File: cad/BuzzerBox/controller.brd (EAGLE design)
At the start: 100 x 100 mm, 132 parts, among them J2 RASPBERRYPI-40-PIN-GPIO_PTH_N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, Q1 BSS138, Q2 BSS138, Q3 BSS138, T1 BC849, T10 BC849, T2 BC849, T3 BC849, T4 BC849, T5 BC849, T6 BC849, T7 BC849, T8 BC849, T9 BC849, U1 ATMEGA328P-AU, Y1 16MHz

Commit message: Pull back internal layers around non plated drill holes
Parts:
- renumbered U$5 to U$4
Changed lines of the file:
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@@
 <element name="U$2" library="WingTechCorner" package="M3-HOLE" value="" x="95" y="95" smashed="yes"/>
 <element name="U$3" library="WingTechCorner" package="M3-HOLE" value="" x="95" y="5" smashed="yes"/>
-<element name="U$5" library="WingTechCorner" package="M3-HOLE" value="" x="5" y="95" smashed="yes"/>
 <element name="7SEG" library="display-kingbright" library_urn="urn:adsk.eagle:library:213" package="SA10-21" package3d_urn="urn:adsk.eagle:package:13078/1" value="7-SEG_SA10-21" x="69.215" y="50.8" smashed="yes" rot="MR0">
 <attribute name="MF" value="" x="94.615" y="88.9" size="1.778" layer="28" rot="MR0" display="off"/>
@@
 <attribute name="VALUE" x="88.519" y="19.939" size="1.27" layer="27"/>
 </element>
+<element name="U$4" library="WingTechCorner" package="M3-HOLE" value="" x="5" y="95" smashed="yes"/>
 </elements>
 <signals>

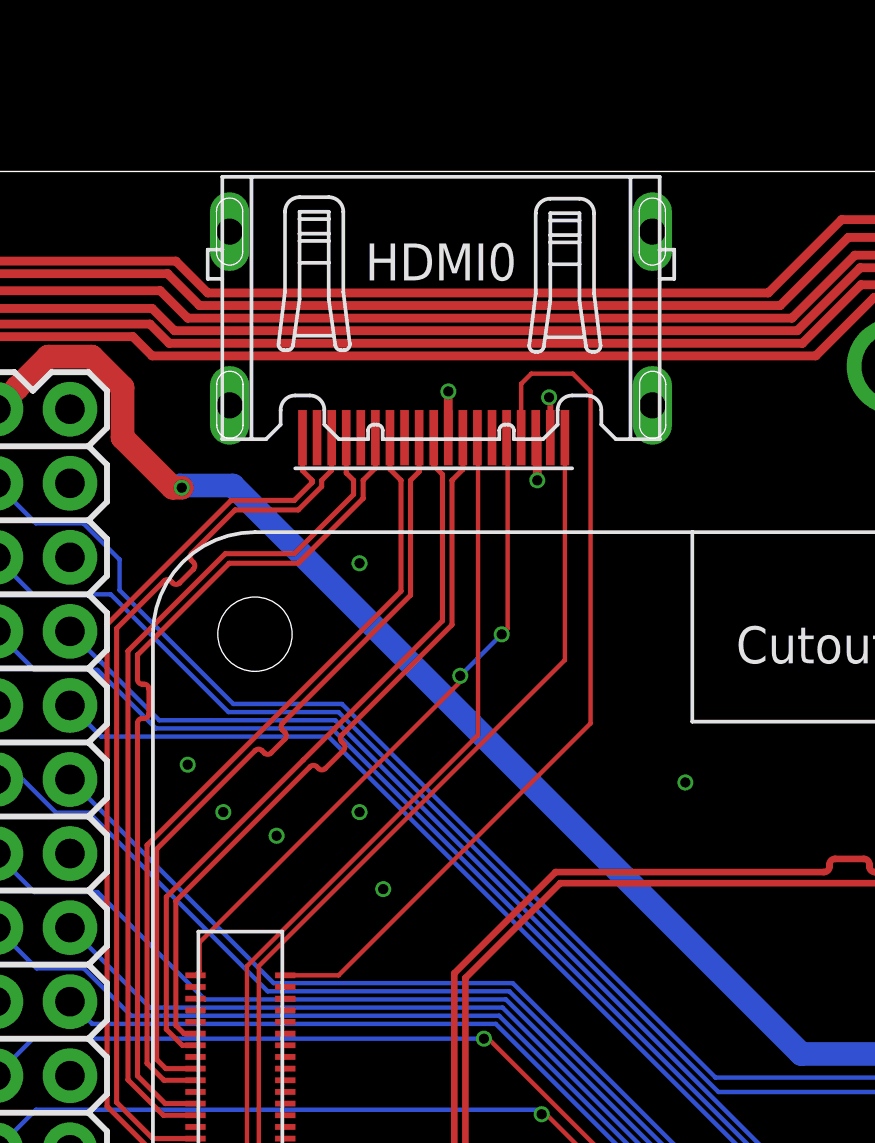
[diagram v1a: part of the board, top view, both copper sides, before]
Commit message: Fix HDMI pin offset
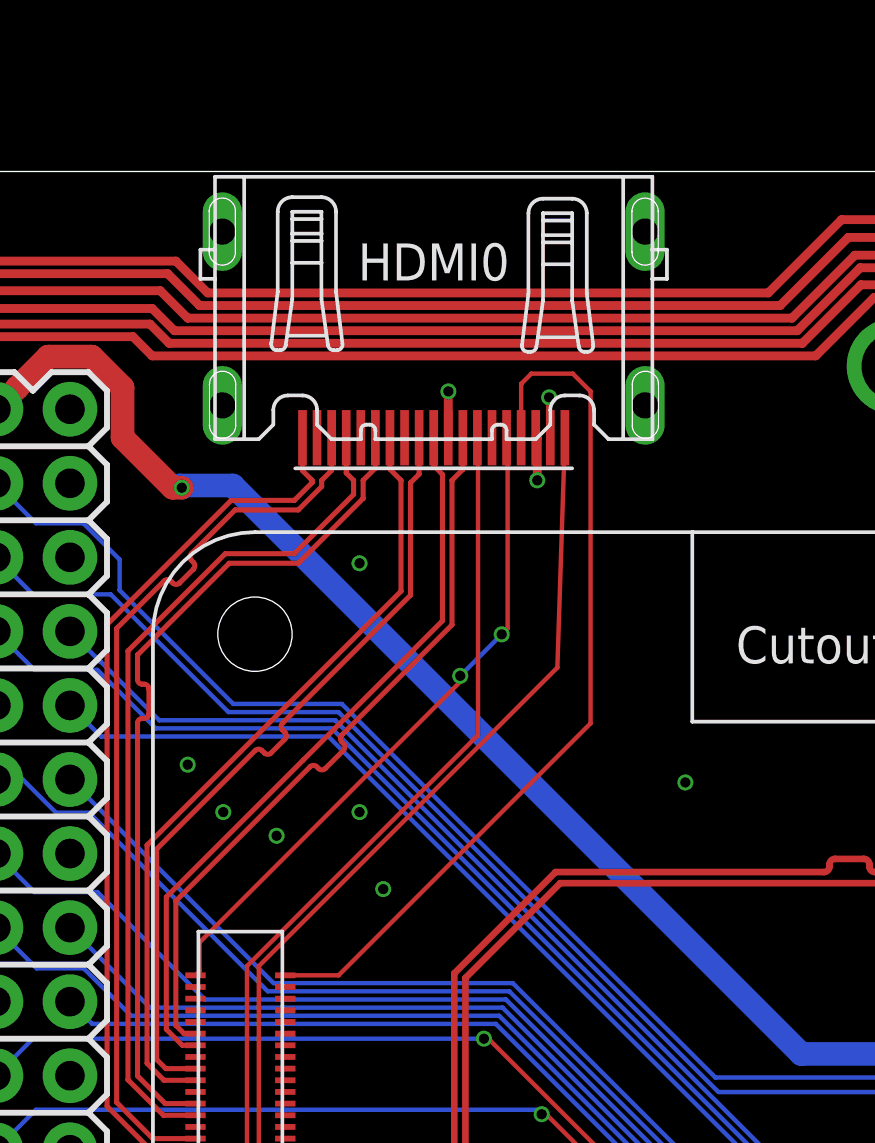
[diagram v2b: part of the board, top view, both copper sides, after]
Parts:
- moved HDMI0 0.25 mm to (30.6, 94.8)
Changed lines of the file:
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@@
 <setting verticaltext="up"/>
 </settings>
-<grid distance="8" unitdist="mil" unit="mil" style="lines" multiple="1" display="yes" altdistance="1" altunitdist="mil" altunit="mil"/>
+<grid distance="0.25" unitdist="mm" unit="mm" style="lines" multiple="1" display="yes" altdistance="1" altunitdist="mil" altunit="mil"/>
 <layers>
 <layer number="1" name="Top" color="4" fill="1" visible="yes" active="yes"/>
@@
 <attribute name="VALUE" x="13.1572" y="93.1164" size="0.6096" layer="27" font="vector" ratio="20" rot="R270"/>
 </element>
-<element name="HDMI0" library="connectors" package="HDMI_A" value="HDMI-A" x="30.8356" y="94.8182" smashed="yes" rot="R180">
-<attribute name="LCSC" value="C138388" x="30.8356" y="94.8182" size="1.778" layer="27" rot="R180" display="off"/>
-<attribute name="NAME" x="30.8356" y="96.8982" size="1.27" layer="25" font="vector" rot="R180" align="center"/>
+<element name="HDMI0" library="connectors" package="HDMI_A" value="HDMI-A" x="30.5856" y="94.8182" smashed="yes" rot="R180">
+<attribute name="LCSC" value="C138388" x="30.5856" y="94.8182" size="1.778" layer="27" rot="R180" display="off"/>
+<attribute name="NAME" x="30.5856" y="96.8982" size="1.27" layer="25" font="vector" rot="R180" align="center"/>
 </element>
 <element name="D1" library="diode" library_urn="urn:adsk.eagle:library:210" package="SMB" package3d_urn="urn:adsk.eagle:package:43404/2" value="" x="90.678" y="23.368" smashed="yes">
@@
 <via x="62.9412" y="21.6408" extent="1-16" drill="0.35"/>
 <via x="63.5508" y="18.288" extent="1-16" drill="0.35"/>
-<wire x1="31.0856" y1="90.8682" x2="31.0856" y2="92.452" width="0.3048" layer="1"/>
-<wire x1="31.0856" y1="92.452" x2="31.0896" y2="92.456" width="0.3048" layer="1"/>
+<wire x1="31.0856" y1="90.8682" x2="31.0856" y2="92.45198125" width="0.3048" layer="1"/>
+<wire x1="31.0896" y1="92.426640625" x2="31.0856" y2="92.45198125" width="0.3048" layer="1"/>
+<wire x1="31.0896" y1="92.426640625" x2="31.0896" y2="92.456" width="0.3048" layer="1"/>
 <via x="31.0896" y="92.456" extent="1-16" drill="0.35"/>
-<wire x1="34.0856" y1="90.8682" x2="34.1376" y2="90.8162" width="0.3048" layer="1"/>
-<wire x1="34.1376" y1="90.8162" x2="34.1376" y2="89.408" width="0.3048" layer="1"/>
+<wire x1="34.0856" y1="90.8682" x2="34.1376" y2="90.85454375" width="0.3048" layer="1"/>
+<wire x1="34.1376" y1="90.85454375" x2="34.1376" y2="89.408" width="0.3048" layer="1"/>
 <via x="34.1376" y="89.408" extent="1-16" drill="0.35"/>
 <wire x1="87.375" y1="70.485" x2="85.7758" y2="70.485" width="0.3048" layer="1"/>
@@
 <wire x1="64.71150625" y1="59.69330625" x2="62.992" y2="59.69330625" width="0.3048" layer="1"/>
 <via x="62.992" y="59.69330625" extent="1-16" drill="0.35"/>
-<wire x1="34.5856" y1="90.8682" x2="34.5856" y2="92.2112" width="0.2032" layer="1"/>
-<wire x1="34.5856" y1="92.2112" x2="34.544" y2="92.2528" width="0.2032" layer="1"/>
+<wire x1="34.5856" y1="90.8682" x2="34.544" y2="91.091675" width="0.2032" layer="1"/>
+<wire x1="34.544" y1="92.2528" x2="34.544" y2="91.091675" width="0.2032" layer="1"/>
 <via x="34.544" y="92.2528" extent="1-16" drill="0.35"/>
 <wire x1="69.0118" y1="17.6784" x2="70.3072" y2="17.6784" width="0.3048" layer="1"/>
@@
 <wire x1="22.415" y1="69.23" x2="21.3972" y2="69.23" width="0.17500625" layer="1"/>
 <wire x1="21.3972" y1="69.23" x2="21.082" y2="69.5452" width="0.17500625" layer="1"/>
-<wire x1="29.79140625" y1="85.46820625" x2="29.79140625" y2="89.408" width="0.17500625" layer="1"/>
-<wire x1="30.0856" y1="89.70219375" x2="30.0856" y2="90.8682" width="0.17500625" layer="1"/>
-<wire x1="29.79140625" y1="89.408" x2="30.0856" y2="89.70219375" width="0.17500625" layer="1"/>
+<wire x1="29.79140625" y1="85.46820625" x2="29.79140625" y2="89.32400625" width="0.17500625" layer="1"/>
+<wire x1="30.0856" y1="90.8682" x2="30.0856" y2="89.6182" width="0.17500625" layer="1"/>
+<wire x1="30.0856" y1="89.6182" x2="29.79140625" y2="89.32400625" width="0.17500625" layer="1"/>
 <wire x1="21.082" y1="76.7588" x2="24.462534375" y2="80.139334375" width="0.17500625" layer="1"/>
 <wire x1="24.462534375" y1="80.139334375" x2="24.694046875" y2="80.139334375" width="0.17500625" layer="1" curve="-90"/>
@@
 <via x="32.9184" y="84.1248" extent="1-16" drill="0.35"/>
 <wire x1="32.9184" y1="84.1248" x2="33.1216" y2="84.328" width="0.1524" layer="1"/>
-<wire x1="33.1216" y1="84.328" x2="33.1216" y2="90.8322" width="0.1524" layer="1"/>
-<wire x1="33.1216" y1="90.8322" x2="33.0856" y2="90.8682" width="0.1524" layer="1"/>
+<wire x1="33.1216" y1="84.328" x2="33.1216" y2="90.86214375" width="0.1524" layer="1"/>
+<wire x1="33.1216" y1="90.86214375" x2="33.0856" y2="90.8682" width="0.1524" layer="1"/>
 </signal>
 <signal name="HDMI_SDA">
@@
 <wire x1="24.1808" y1="63.3984" x2="24.1808" y2="72.7456" width="0.1524" layer="1"/>
 <wire x1="24.1808" y1="72.7456" x2="32.1056" y2="80.6704" width="0.1524" layer="1"/>
-<wire x1="32.1056" y1="90.8482" x2="32.0856" y2="90.8682" width="0.1524" layer="1"/>
-<wire x1="32.1056" y1="80.6704" x2="32.1056" y2="90.8482" width="0.1524" layer="1"/>
+<wire x1="32.1056" y1="90.866459375" x2="32.0856" y2="90.8682" width="0.1524" layer="1"/>
+<wire x1="32.1056" y1="80.6704" x2="32.1056" y2="90.866459375" width="0.1524" layer="1"/>
 </signal>
 <signal name="HDMI_HOT">
@@
 <wire x1="25.15835625" y1="63.23" x2="24.9423125" y2="63.44604375" width="0.1524" layer="1"/>
 <wire x1="24.5872" y1="63.8048" x2="24.5872" y2="72.7456" width="0.1524" layer="1"/>
-<wire x1="35.0856" y1="83.244" x2="35.0856" y2="90.8682" width="0.1524" layer="1"/>
-<wire x1="24.5872" y1="72.7456" x2="35.0856" y2="83.244" width="0.1524" layer="1"/>
+<wire x1="34.827125" y1="82.985525" x2="35.0856" y2="90.8682" width="0.1524" layer="1"/>
+<wire x1="24.5872" y1="72.7456" x2="34.827125" y2="82.985525" width="0.1524" layer="1"/>
 </signal>
 <signal name="GP4">

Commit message: Added missing trace
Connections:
- removed net D12: C7.1, R2.2, R3.1
- net A1: now also C7.1, R2.2, R3.1
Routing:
- net A1: track 0.00 -> 58.2 mm, vias 0 -> 4
- net D12: track 5.26 -> 0.00 mm
- net D6: track 38.1 -> 35.3 mm
- net D5: track 33.1 -> 30.3 mm
- net D3: track 27.1 -> 26.3 mm
- net D4: track 30.2 -> 29.4 mm
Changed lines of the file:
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@@
 <setting verticaltext="up"/>
 </settings>
-<grid distance="0.25" unitdist="mm" unit="mm" style="lines" multiple="1" display="yes" altdistance="1" altunitdist="mil" altunit="mil"/>
+<grid distance="25" unitdist="mil" unit="mil" style="lines" multiple="1" display="yes" altdistance="1" altunitdist="mil" altunit="mil"/>
 <layers>
 <layer number="1" name="Top" color="4" fill="1" visible="yes" active="yes"/>
@@
 <attribute name="MF" value="" x="92.069" y="30.645" size="1.778" layer="27" rot="R90" display="off"/>
 <attribute name="MPN" value="" x="92.069" y="30.645" size="1.778" layer="27" rot="R90" display="off"/>
-<attribute name="NAME" x="94.9265" y="26.54" size="1.27" layer="25" rot="R180"/>
+<attribute name="NAME" x="86.46" y="33.6765" size="1.27" layer="25" rot="R270"/>
 <attribute name="OC_FARNELL" value="unknown" x="92.069" y="30.645" size="1.778" layer="27" rot="R90" display="off"/>
 <attribute name="OC_NEWARK" value="unknown" x="92.069" y="30.645" size="1.778" layer="27" rot="R90" display="off"/>
@@
 </element>
 <element name="D1" library="diode" library_urn="urn:adsk.eagle:library:210" package="SMB" package3d_urn="urn:adsk.eagle:package:43404/2" value="" x="90.678" y="23.368" smashed="yes">
-<attribute name="NAME" x="88.519" y="25.527" size="1.27" layer="25"/>
+<attribute name="NAME" x="89.769" y="20.027" size="1.27" layer="25"/>
 <attribute name="POPULARITY" value="3" x="90.678" y="23.368" size="1.778" layer="27" display="off"/>
 <attribute name="VALUE" x="88.519" y="19.939" size="1.27" layer="27"/>
@@
 <wire x1="12.1666" y1="38.481" x2="40.894" y2="38.481" width="0.3048" layer="1"/>
 </signal>
-<signal name="D12">
-<contactref element="R3" pad="1"/>
-<contactref element="R2" pad="2"/>
-<contactref element="C7" pad="1"/>
-<wire x1="27.94" y1="21.148" x2="27.244" y2="21.844" width="0.3048" layer="1"/>
-<wire x1="27.244" y1="21.844" x2="25.665" y2="21.844" width="0.3048" layer="1"/>
-<wire x1="25.665" y1="21.844" x2="23.76" y2="23.749" width="0.3048" layer="1"/>
-</signal>
 <signal name="N$3">
 <contactref element="R2" pad="1"/>
@@
 <wire x1="60.5282" y1="21.6916" x2="55.9816" y2="21.6916" width="0.3048" layer="1"/>
 <wire x1="55.245" y1="15.875" x2="54.61" y2="15.24" width="0.3048" layer="1"/>
-<wire x1="54.61" y1="15.24" x2="45.72" y2="15.24" width="0.3048" layer="1"/>
-<wire x1="44.892" y1="16.068" x2="44.892" y2="17.78" width="0.3048" layer="1"/>
+<wire x1="54.61" y1="15.24" x2="46.99" y2="15.24" width="0.3048" layer="1"/>
+<wire x1="44.892" y1="17.338" x2="44.892" y2="17.78" width="0.3048" layer="1"/>
 <wire x1="55.9816" y1="21.6916" x2="55.245" y2="20.955" width="0.3048" layer="1"/>
 <wire x1="55.245" y1="20.955" x2="55.245" y2="15.875" width="0.3048" layer="1"/>
-<wire x1="45.72" y1="15.24" x2="44.892" y2="16.068" width="0.3048" layer="1"/>
+<wire x1="46.99" y1="15.24" x2="44.892" y2="17.338" width="0.3048" layer="1"/>
 </signal>
 <signal name="N$9">
@@
 <wire x1="38.928" y1="17.78" x2="38.928" y2="19.878" width="0.3048" layer="1"/>
 <wire x1="38.928" y1="19.878" x2="38.9526" y2="19.9026" width="0.3048" layer="1"/>
-<wire x1="61.976" y1="15.4432" x2="61.976" y2="14.8082" width="0.3048" layer="1"/>
-<wire x1="61.976" y1="14.8082" x2="61.1378" y2="13.97" width="0.3048" layer="1"/>
-<wire x1="61.1378" y1="13.97" x2="39.37" y2="13.97" width="0.3048" layer="1"/>
-<wire x1="38.928" y1="17.78" x2="38.928" y2="14.412" width="0.3048" layer="1"/>
-<wire x1="38.928" y1="14.412" x2="39.37" y2="13.97" width="0.3048" layer="1"/>
+<wire x1="41.91" y1="14.605" x2="60.96" y2="14.605" width="0.3048" layer="1"/>
+<wire x1="38.928" y1="17.78" x2="38.928" y2="17.587" width="0.3048" layer="1"/>
+<wire x1="38.928" y1="17.587" x2="41.91" y2="14.605" width="0.3048" layer="1"/>
+<wire x1="60.96" y1="14.605" x2="61.7982" y2="15.4432" width="0.3048" layer="1"/>
+<wire x1="61.7982" y1="15.4432" x2="61.976" y2="15.4432" width="0.3048" layer="1"/>
 </signal>
 <signal name="N$12">
@@
 <wire x1="35.93" y1="18.614" x2="35.93" y2="19.9026" width="0.3048" layer="1"/>
 <wire x1="35.93" y1="19.9026" x2="35.93" y2="20.055" width="0.3048" layer="1"/>
-<wire x1="62.7634" y1="15.4432" x2="62.7634" y2="13.8684" width="0.3048" layer="1"/>
-<wire x1="62.7634" y1="13.8684" x2="62.23" y2="13.335" width="0.3048" layer="1"/>
-<wire x1="62.23" y1="13.335" x2="37.465" y2="13.335" width="0.3048" layer="1"/>
+<wire x1="40.005" y1="13.97" x2="62.23" y2="13.97" width="0.3048" layer="1"/>
 <wire x1="36.764" y1="17.78" x2="36.83" y2="17.714" width="0.3048" layer="1"/>
-<wire x1="36.83" y1="17.714" x2="36.83" y2="13.97" width="0.3048" layer="1"/>
-<wire x1="36.83" y1="13.97" x2="37.465" y2="13.335" width="0.3048" layer="1"/>
+<wire x1="36.83" y1="17.714" x2="36.83" y2="17.145" width="0.3048" layer="1"/>
+<wire x1="36.83" y1="17.145" x2="40.005" y2="13.97" width="0.3048" layer="1"/>
+<wire x1="62.23" y1="13.97" x2="62.7634" y2="14.5034" width="0.3048" layer="1"/>
+<wire x1="62.7634" y1="14.5034" x2="62.7634" y2="15.4432" width="0.3048" layer="1"/>
 </signal>
 <signal name="N$15">
@@
 <contactref element="MCP1" pad="28"/>
 <contactref element="R42" pad="1"/>
-<wire x1="82.18" y1="56.515" x2="82.815" y2="55.88" width="0.3048" layer="1"/>
-<wire x1="86.74" y1="55.88" x2="87.375" y2="55.245" width="0.3048" layer="1"/>
-<wire x1="82.815" y1="55.88" x2="86.74" y2="55.88" width="0.3048" layer="1"/>
+<wire x1="82.18" y1="56.515" x2="83.315" y2="55.38" width="0.3048" layer="1"/>
+<wire x1="87.24" y1="55.38" x2="87.375" y2="55.245" width="0.3048" layer="1"/>
+<wire x1="83.315" y1="55.38" x2="87.24" y2="55.38" width="0.3048" layer="1"/>
 </signal>
 <signal name="D">
@@
 <wire x1="54.61" y1="21.59" x2="54.61" y2="16.51" width="0.3048" layer="1"/>
 <wire x1="54.61" y1="16.51" x2="53.975" y2="15.875" width="0.3048" layer="1"/>
-<wire x1="53.975" y1="15.875" x2="47.625" y2="15.875" width="0.3048" layer="1"/>
-<wire x1="47.625" y1="15.875" x2="46.99" y2="16.51" width="0.3048" layer="1"/>
-<wire x1="46.99" y1="16.51" x2="46.99" y2="17.714" width="0.3048" layer="1"/>
-<wire x1="46.99" y1="17.714" x2="47.056" y2="17.78" width="0.3048" layer="1"/>
+<wire x1="53.975" y1="15.875" x2="48.895" y2="15.875" width="0.3048" layer="1"/>
+<wire x1="48.895" y1="15.875" x2="47.023" y2="17.747" width="0.3048" layer="1"/>
+<wire x1="47.023" y1="17.747" x2="47.056" y2="17.78" width="0.3048" layer="1"/>
 </signal>
 <signal name="A1">
 <contactref element="U1" pad="24"/>
+<contactref element="R3" pad="1"/>
+<contactref element="R2" pad="2"/>
+<contactref element="C7" pad="1"/>
+<wire x1="27.94" y1="21.148" x2="27.244" y2="21.844" width="0.3048" layer="1"/>
+<wire x1="27.244" y1="21.844" x2="25.665" y2="21.844" width="0.3048" layer="1"/>
+<wire x1="25.665" y1="21.844" x2="23.76" y2="23.749" width="0.3048" layer="1"/>
+<wire x1="27.94" y1="21.148" x2="28.133" y2="20.955" width="0.3048" layer="1"/>
+<wire x1="28.133" y1="20.955" x2="29.21" y2="20.955" width="0.3048" layer="1"/>
+<via x="29.21" y="20.955" extent="1-16" drill="0.35"/>
+<wire x1="29.21" y1="20.955" x2="31.75" y2="20.955" width="0.3048" layer="16"/>
+<via x="31.75" y="20.955" extent="1-16" drill="0.35"/>
+<wire x1="31.75" y1="20.955" x2="32.385" y2="20.32" width="0.3048" layer="1"/>
+<wire x1="32.385" y1="13.97" x2="33.02" y2="13.335" width="0.3048" layer="1"/>
+<wire x1="32.385" y1="20.32" x2="32.385" y2="13.97" width="0.3048" layer="1"/>
+<wire x1="33.02" y1="13.335" x2="59.69" y2="13.335" width="0.3048" layer="1"/>
+<via x="59.69" y="13.335" extent="1-16" drill="0.35"/>
+<wire x1="59.69" y1="13.335" x2="66.04" y2="19.685" width="0.3048" layer="16"/>
+<via x="66.04" y="19.685" extent="1-16" drill="0.35"/>
+<wire x1="66.04" y1="19.685" x2="66.04" y2="21.59" width="0.3048" layer="1"/>
+<wire x1="66.04" y1="21.59" x2="66.929" y2="22.479" width="0.3048" layer="1"/>
+<wire x1="69.0118" y1="22.479" x2="66.929" y2="22.479" width="0.3048" layer="1"/>
 </signal>
 <signal name="A2">
@@
 <wire x1="25.15835625" y1="63.23" x2="24.9423125" y2="63.44604375" width="0.1524" layer="1"/>
 <wire x1="24.5872" y1="63.8048" x2="24.5872" y2="72.7456" width="0.1524" layer="1"/>
-<wire x1="34.827125" y1="82.985525" x2="35.0856" y2="90.8682" width="0.1524" layer="1"/>
-<wire x1="24.5872" y1="72.7456" x2="34.827125" y2="82.985525" width="0.1524" layer="1"/>
+<wire x1="35.0856" y1="83.493984375" x2="35.0856" y2="90.8682" width="0.1524" layer="1"/>
+<wire x1="35.0856" y1="83.493984375" x2="35.077125" y2="83.235525" width="0.1524" layer="1"/>
+<wire x1="24.5872" y1="72.7456" x2="35.077125" y2="83.235525" width="0.1524" layer="1"/>
 </signal>
 <signal name="GP4">
